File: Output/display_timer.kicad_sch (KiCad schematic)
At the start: 7 parts, among them U5 NE555P, U6 CD74HCT139E, U7 CD74HCT73E

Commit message: Output PCB routed
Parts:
- C2, C3: footprint (none) -> _DownloadFootprints:Cp_2mm_pin_spacing
- R1, R2: footprint (none) -> _DownloadFootprints:CF_series_Resistors_THT
- U6: footprint (none) -> _DownloadFootprints:2x_2_to_4_demux
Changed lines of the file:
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@@
 			)
 		)
-		(property "Footprint" ""
+		(property "Footprint" "_DownloadFootprints:CF_series_Resistors_THT"
 			(at 86.36 56.642 90)
 			(effects
@@
 			)
 		)
-		(property "Footprint" ""
+		(property "Footprint" "_DownloadFootprints:2x_2_to_4_demux"
 			(at 67.31 101.6 0)
 			(effects
@@
 			)
 		)
-		(property "Footprint" ""
+		(property "Footprint" "_DownloadFootprints:CF_series_Resistors_THT"
 			(at 76.2 56.642 90)
 			(effects
@@
 			)
 		)
-		(property "Footprint" ""
+		(property "Footprint" "_DownloadFootprints:Cp_2mm_pin_spacing"
 			(at 41.91 47.2948 0)
 			(effects
@@
 			)
 		)
-		(property "Footprint" ""
+		(property "Footprint" "_DownloadFootprints:Cp_2mm_pin_spacing"
 			(at 41.91 54.3052 0)
 			(effects

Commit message: Added silkscreen to IO and added edge cuts and mounting points
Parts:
- C2, C3: footprint _DownloadFootprints:Cp_2mm_pin_spacing -> Capacitor_THT:C_Disc_D5.0mm_W2.5mm_P2.50mm
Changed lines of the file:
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@@
 			)
 		)
-		(property "Footprint" "_DownloadFootprints:Cp_2mm_pin_spacing"
+		(property "Footprint" "Capacitor_THT:C_Disc_D5.0mm_W2.5mm_P2.50mm"
 			(at 41.91 47.2948 0)
 			(effects
@@
 			)
 		)
-		(property "Footprint" "_DownloadFootprints:Cp_2mm_pin_spacing"
+		(property "Footprint" "Capacitor_THT:C_Disc_D5.0mm_W2.5mm_P2.50mm"
 			(at 41.91 54.3052 0)
 			(effects

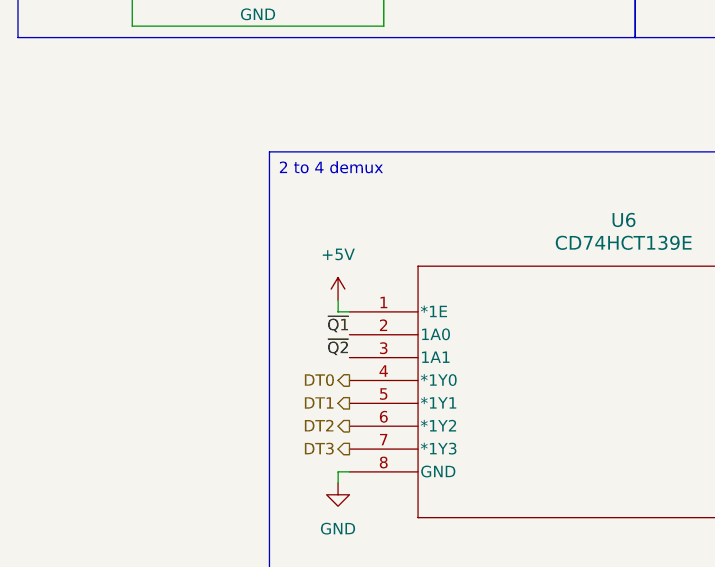
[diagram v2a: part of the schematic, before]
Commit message: Demux enable is active low. Should have been connected to ground not power
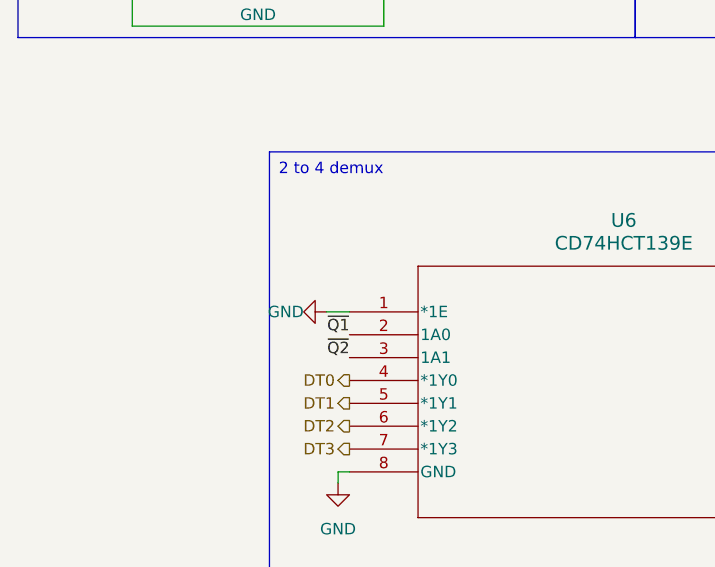
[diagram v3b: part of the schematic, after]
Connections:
- net +5V: no longer U6.1 (*1E)
- net GND: now also U6.1 (*1E)
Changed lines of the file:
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@@
-	(wire
-		(pts
-			(xy 66.04 101.6) (xy 67.31 101.6)
-		)
-		(stroke
-			(width 0)
-			(type default)
-		)
-	)
 	(wire
 		(pts
@@
 	(wire
 		(pts
-			(xy 66.04 100.33) (xy 66.04 101.6)
-		)
-		(stroke
-			(width 0)
-			(type default)
-		)
-	)
-	(wire
-		(pts
 			(xy 91.44 58.42) (xy 90.17 58.42)
 		)
@@
 		(pts
 			(xy 168.91 58.42) (xy 168.91 48.26)
+		)
+		(stroke
+			(width 0)
+			(type default)
+		)
+	)
+	(wire
+		(pts
+			(xy 64.77 101.6) (xy 67.31 101.6)
 		)
 		(stroke
@@
 				(path "/02a99fb8-2048-4cc8-b7aa-813268289b08/c1c66350-f8ad-4109-81b0-a0d7296f9bbf"
 					(reference "R2")
+					(unit 1)
+				)
+			)
+		)
+	)
+	(symbol
+		(lib_id "power:GND")
+		(at 64.77 101.6 270)
+		(unit 1)
+		(exclude_from_sim no)
+		(in_bom yes)
+		(on_board yes)
+		(dnp no)
+		(property "Reference" "#PWR017"
+			(at 58.42 101.6 0)
+			(effects
+				(font
+					(size 1.27 1.27)
+				)
+				(hide yes)
+			)
+		)
+		(property "Value" "GND"
+			(at 62.23 101.6 90)
+			(effects
+				(font
+					(size 1.27 1.27)
+				)
+				(justify right)
+			)
+		)
+		(property "Footprint" ""
+			(at 64.77 101.6 0)
+			(effects
+				(font
+					(size 1.27 1.27)
+				)
+				(hide yes)
+			)
+		)
+		(property "Datasheet" ""
+			(at 64.77 101.6 0)
+			(effects
+				(font
+					(size 1.27 1.27)
+				)
+				(hide yes)
+			)
+		)
+		(property "Description" "Power symbol creates a global label with name \"GND\" , ground"
+			(at 64.77 101.6 0)
+			(effects
+				(font
+					(size 1.27 1.27)
+				)
+				(hide yes)
+			)
+		)
+		(pin "1"
+		)
+		(instances
+			(project ""
+				(path "/02a99fb8-2048-4cc8-b7aa-813268289b08/c1c66350-f8ad-4109-81b0-a0d7296f9bbf"
+					(reference "#PWR017")
 					(unit 1)
 				)
@@
 					(unit 1)
 				)
-			)
-		)
-	)
-	(symbol
-		(lib_id "power:+5V")
-		(at 66.04 100.33 0)
-		(unit 1)
-		(exclude_from_sim no)
-		(in_bom yes)
-		(on_board yes)
-		(dnp no)
-		(fields_autoplaced yes)
-		(property "Reference" "#PWR017"
-			(at 66.04 104.14 0)
-			(effects
-				(font
-					(size 1.27 1.27)
-				)
-				(hide yes)
-			)
-		)
-		(property "Value" "+5V"
-			(at 66.04 95.25 0)
-			(effects
-				(font
-					(size 1.27 1.27)
-				)
-			)
-		)
-		(property "Footprint" ""
-			(at 66.04 100.33 0)
-			(effects
-				(font
-					(size 1.27 1.27)
-				)
-				(hide yes)
-			)
-		)
-		(property "Datasheet" ""
-			(at 66.04 100.33 0)
-			(effects
-				(font
-					(size 1.27 1.27)
-				)
-				(hide yes)
-			)
-		)
-		(property "Description" "Power symbol creates a global label with name \"+5V\""
-			(at 66.04 100.33 0)
-			(effects
-				(font
-					(size 1.27 1.27)
-				)
-				(hide yes)
-			)
-		)
-		(pin "1"
-		)
-		(instances
-			(project "Output"
-				(path "/02a99fb8-2048-4cc8-b7aa-813268289b08/c1c66350-f8ad-4109-81b0-a0d7296f9bbf"
-					(reference "#PWR017")
-					(unit 1)
-				)
